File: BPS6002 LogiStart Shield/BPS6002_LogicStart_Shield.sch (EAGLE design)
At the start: 83 parts, among them J1 AUDIO-CONNECTOR-6P-SMD-344003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, Q1 MMBTA56, Q2 MMBTA56, Q3 MMBTA56, Q4 MMBTA56, Q5 MMBTA56

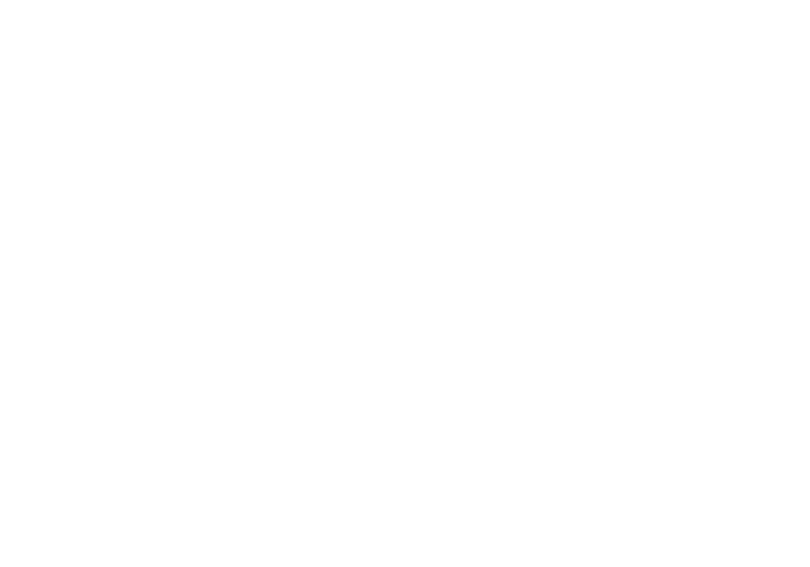
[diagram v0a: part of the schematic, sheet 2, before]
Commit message: Added GPIO Header
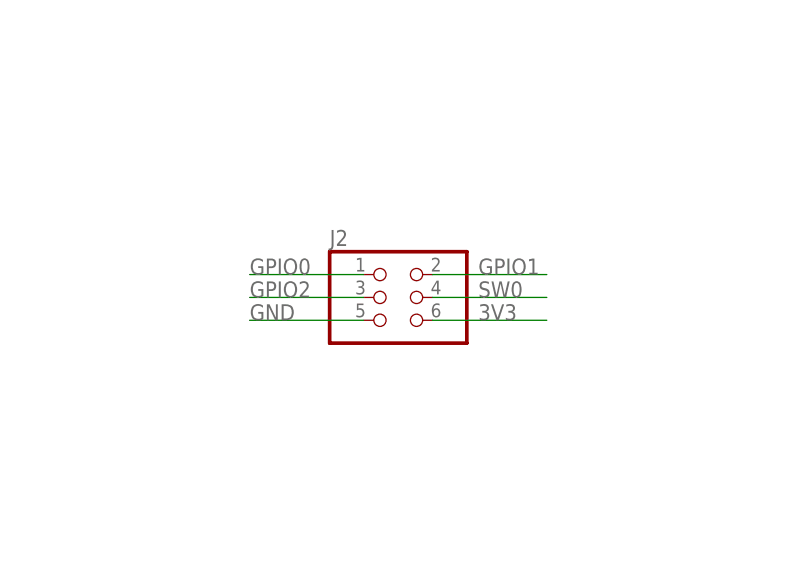
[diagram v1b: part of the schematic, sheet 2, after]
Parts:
- added J2: (no value), pinhead:PINHD-2X3
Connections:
- removed net NC1: H1.D48
- removed net NC2: H1.D50
- removed net NC3: H1.D52
- new net GPIO0: H1.D26, J2.1
- new net GPIO1: H1.D28, J2.2
- new net GPIO2: H1.D30, J2.3
- net 3V3: now also J2.6
- net GND: now also J2.5
- net LED0: now also H1.D48; no longer H1.D42
- net LED1: now also H1.D50; no longer H1.D44
- net LED2: now also H1.D52; no longer H1.D46
- net SW0: now also H1.D32, J2.4; no longer H1.D26
- net SW1: now also H1.D34; no longer H1.D28
- net SW2: now also H1.D36; no longer H1.D30
- net SW3: now also H1.D38; no longer H1.D32
- net SW4: now also H1.D40; no longer H1.D34
- net SW5: now also H1.D42; no longer H1.D36
- net SW6: now also H1.D44; no longer H1.D38
- net SW7: now also H1.D46; no longer H1.D40

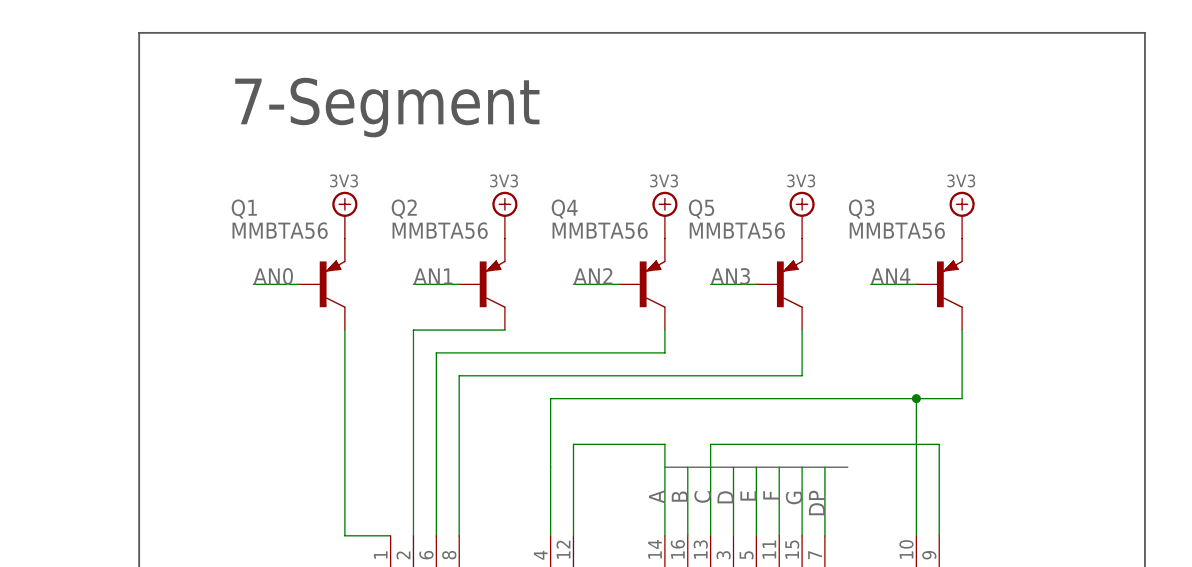
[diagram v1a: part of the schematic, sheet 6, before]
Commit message: LogicStart Shield with Joystick generic header
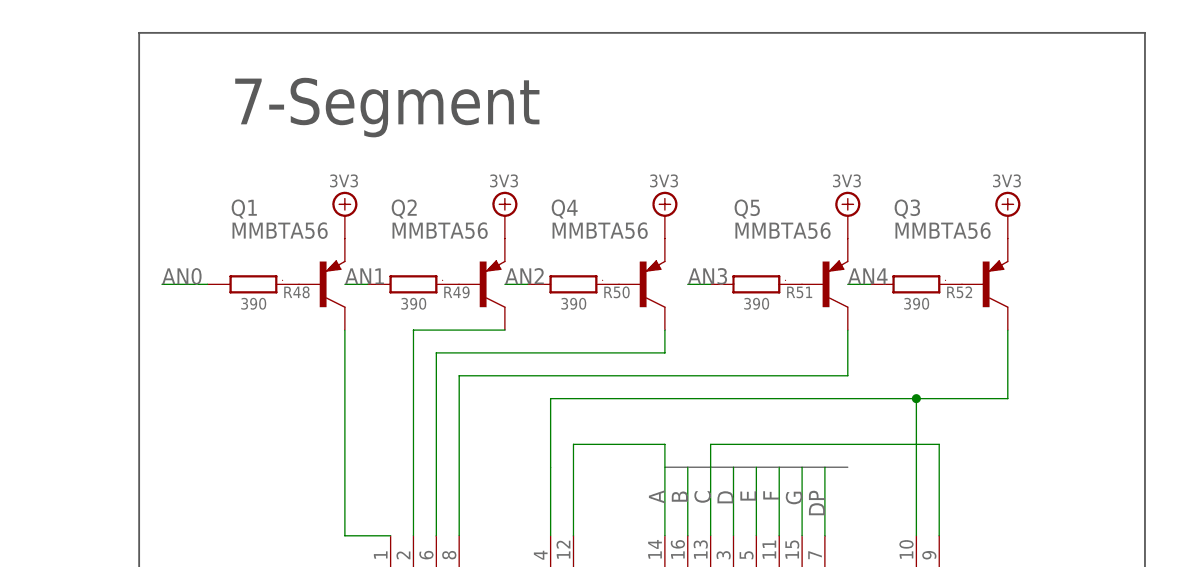
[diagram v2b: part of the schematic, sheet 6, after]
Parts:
- added J3: (no value), pinhead:PINHD-2X3
- added R48, R49, R50, R51, R52: 390, GadgetFactory:R0603
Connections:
- new net N$2: Q1.B, R48A.1
- new net N$3: Q2.B, R49A.1
- new net N$6: Q4.B, R50A.1
- new net N$7: Q5.B, R51A.1
- new net N$8: Q3.B, R52A.1
- net AN0: now also H1.D40, R48A.2; no longer H1.*D3, Q1.B
- net AN1: now also H1.D38, R49A.2; no longer H1.*D2, Q2.B
- net AN2: now also H1.D34, R50A.2; no longer H1.RX, Q4.B
- net AN3: now also H1.D32, R51A.2; no longer H1.D4, Q5.B
- net AN4: now also H1.D36, R52A.2; no longer H1.TX, Q3.B
- net DIR_DOWN: now also J3.4
- net DIR_LEFT: now also J3.3
- net DIR_RIGHT: now also J3.1
- net DIR_UP: now also J3.2
- net GND: now also J3.5
- net SW0: now also H1.RX; no longer H1.D32
- net SW1: now also H1.TX; no longer H1.D34
- net SW2: now also H1.*D2; no longer H1.D36
- net SW3: now also H1.*D3; no longer H1.D38
- net SW4: now also H1.D4; no longer H1.D40
- net SW7: now also J3.6
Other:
- moved on the sheet: Q3, Q5

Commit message: LogicStart Shield
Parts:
- removed J3: (no value), pinhead:PINHD-2X3
- added W1: WING8_NOHOLES_FEMALE_TOP, Papilio:WING8WING8_NOHOLES
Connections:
- net 3V3: now also W1.3V3
- net 5V0: now also W1.5V
- net DIR_DOWN: no longer J3.4
- net DIR_LEFT: no longer J3.3
- net DIR_RIGHT: no longer J3.1
- net DIR_UP: no longer J3.2
- net GND: now also W1.GND; no longer J3.5
- net SW0: now also W1.8
- net SW1: now also W1.7
- net SW2: now also W1.6
- net SW3: now also W1.5
- net SW4: now also W1.4
- net SW5: now also W1.3
- net SW6: now also W1.2
- net SW7: now also W1.1; no longer J3.6

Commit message: LogicStart Shield V1.01
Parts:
- added AREF: (no value), adafruit:PINHD-1X1
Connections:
- new net N$9: AREF.1, H1.AREF
- net 3V3: now also JP2.1, JP2.2, JP2.3, JP2.4, JP2.5, JP2.6
- net 5V0: no longer H1.AREF, JP2.1, JP2.2, JP2.3, JP2.4, JP2.5, JP2.6
